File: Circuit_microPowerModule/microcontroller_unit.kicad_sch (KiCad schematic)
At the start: 34 parts, among them J1 USB_C_Receptacle_USB2.0, J5 Debug, SW2 KMR2, SW3 KMR2, U6 RP2040, U9 W25Q128JVS, Y1 12MHz

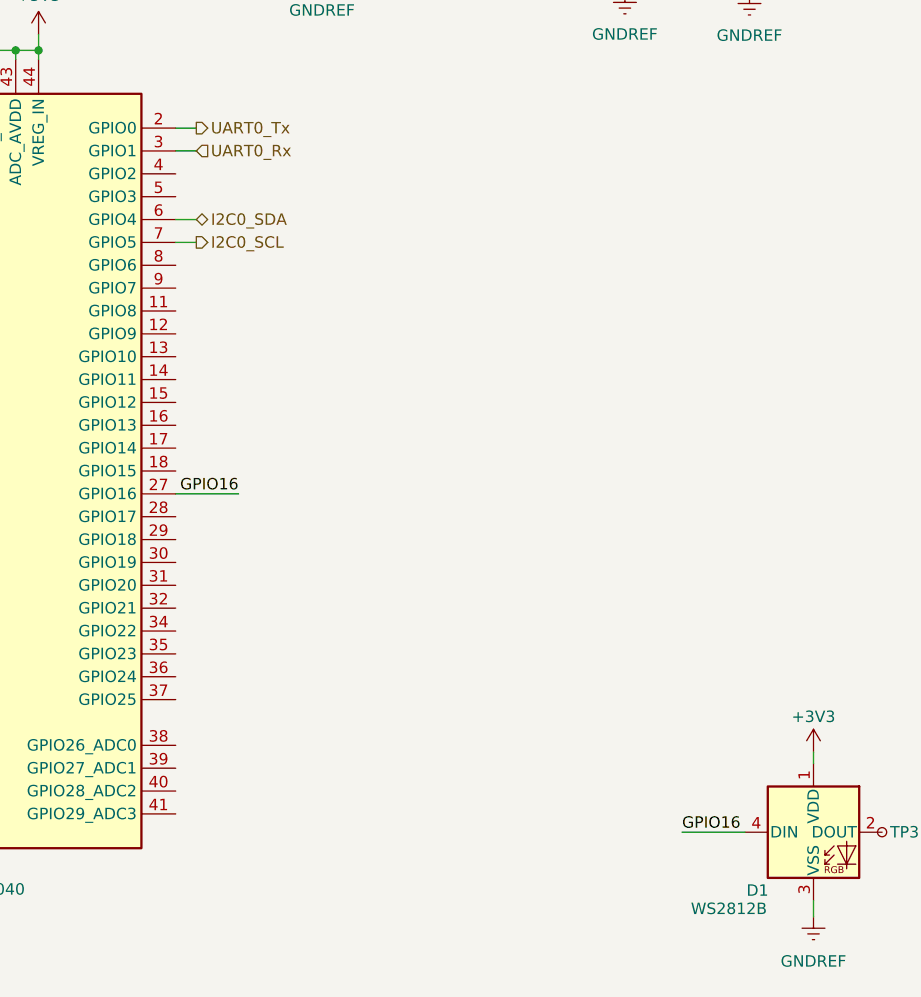
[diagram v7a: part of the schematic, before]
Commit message: define mcu pinout to mikrobus
update hw block diagram file type
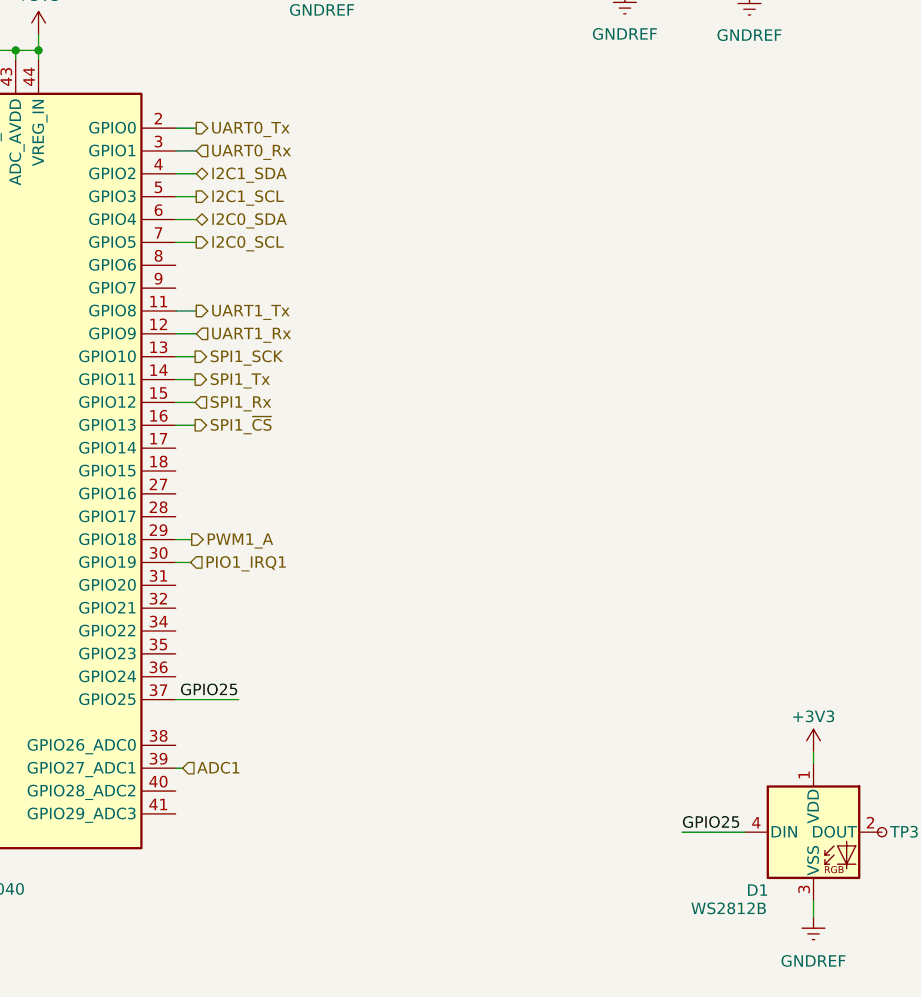
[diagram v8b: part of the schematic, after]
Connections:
- net UART1_Tx: now reaches U6.11 (GPIO8)
- net UART1_Rx: now reaches U6.12 (GPIO9)
- net SPI1_SCK: now reaches U6.13 (GPIO10)
- net SPI1_Tx: now reaches U6.14 (GPIO11)
- net SPI1_Rx: now reaches U6.15 (GPIO12)
- net SPI1_~{CS}: now reaches U6.16 (GPIO13)
- net PWM1_A: now reaches U6.29 (GPIO18)
- net PIO1_IRQ1: now reaches U6.30 (GPIO19)
- net GPIO25: now reaches U6.37 (GPIO25)
- net GPIO25: now also D1.4 (DIN)
- net ADC1: now reaches U6.39 (GPIO27_ADC1)
- net I2C1_SDA: now reaches U6.4 (GPIO2)
- net I2C1_SCL: now reaches U6.5 (GPIO3)
- net GPIO16: no longer names the net of U6.27 (GPIO16)
- net GPIO16: no longer D1.4 (DIN)
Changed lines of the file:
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@@
+    (stroke (width 0) (type default))
+  )
+  (wire (pts (xy 195.834 71.374) (xy 198.12 71.374))
     (stroke (width 0) (type default))
   )
@@
     (stroke (width 0) (type default))
   )
+  (wire (pts (xy 195.834 84.074) (xy 197.993 84.074))
+    (stroke (width 0) (type default))
+  )
   (wire (pts (xy 60.96 119.38) (xy 72.009 119.38))
     (stroke (width 0) (type default))
@@
     (stroke (width 0) (type default))
   )
+  (wire (pts (xy 195.834 96.774) (xy 197.612 96.774))
+    (stroke (width 0) (type default))
+  )
   (wire (pts (xy 161.29 24.13) (xy 165.1 24.13))
     (stroke (width 0) (type default))
@@
     (stroke (width 0) (type default))
   )
+  (wire (pts (xy 195.834 81.534) (xy 197.993 81.534))
+    (stroke (width 0) (type default))
+  )
   (wire (pts (xy 60.96 121.92) (xy 72.009 121.92))
     (stroke (width 0) (type default))
@@
     (stroke (width 0) (type default))
   )
+  (wire (pts (xy 195.834 58.674) (xy 198.12 58.674))
+    (stroke (width 0) (type default))
+  )
   (wire (pts (xy 151.13 24.13) (xy 157.48 24.13))
     (stroke (width 0) (type default))
@@
     (stroke (width 0) (type default))
   )
+  (wire (pts (xy 195.834 73.914) (xy 198.12 73.914))
+    (stroke (width 0) (type default))
+  )
   (wire (pts (xy 48.895 23.368) (xy 48.895 24.765))
     (stroke (width 0) (type default))
@@
     (stroke (width 0) (type default))
   )
+  (wire (pts (xy 195.834 122.174) (xy 196.596 122.174))
+    (stroke (width 0) (type default))
+  )
+  (wire (pts (xy 195.834 56.134) (xy 198.12 56.134))
+    (stroke (width 0) (type default))
+  )
   (wire (pts (xy 151.13 22.86) (xy 151.13 24.13))
     (stroke (width 0) (type default))
@@
     (stroke (width 0) (type default))
   )
+  (wire (pts (xy 195.834 78.994) (xy 197.993 78.994))
+    (stroke (width 0) (type default))
+  )
   (wire (pts (xy 195.834 51.054) (xy 198.12 51.054))
     (stroke (width 0) (type default))
@@
     (stroke (width 0) (type default))
   )
+  (wire (pts (xy 195.834 99.314) (xy 197.485 99.314))
+    (stroke (width 0) (type default))
+  )
   (wire (pts (xy 60.96 109.22) (xy 61.849 109.22))
     (stroke (width 0) (type default))
@@
     (stroke (width 0) (type default))
   )
+  (wire (pts (xy 195.834 76.454) (xy 197.993 76.454))
+    (stroke (width 0) (type default))
+  )
   (wire (pts (xy 151.13 31.75) (xy 157.48 31.75))
     (stroke (width 0) (type default))
@@
     (stroke (width 0) (type default))
   )
+  (wire (pts (xy 195.834 114.554) (xy 202.819 114.554))
+    (stroke (width 0) (type default))
+  )
   (wire (pts (xy 145.034 119.634) (xy 137.16 119.634))
     (stroke (width 0) (type default))
@@
   )
   (wire (pts (xy 157.48 31.75) (xy 161.29 31.75))
-    (stroke (width 0) (type default))
-  )
-  (wire (pts (xy 195.834 91.694) (xy 202.819 91.694))
     (stroke (width 0) (type default))
   )
@@
     (effects (font (size 1.27 1.27)) (justify left bottom))
   )
-  (label "GPIO16" (at 202.819 91.694 180) (fields_autoplaced)
-    (effects (font (size 1.27 1.27)) (justify right bottom))
-  )
   (label "SWDIO" (at 137.16 119.634 0) (fields_autoplaced)
     (effects (font (size 1.27 1.27)) (justify left bottom))
@@
     (effects (font (size 1.27 1.27)) (justify right bottom))
   )
-  (label "GPIO16" (at 252.095 129.286 0) (fields_autoplaced)
+  (label "GPIO25" (at 252.095 129.286 0) (fields_autoplaced)
     (effects (font (size 1.27 1.27)) (justify left bottom))
   )
@@
     (effects (font (size 1.27 1.27)) (justify right bottom))
   )
+  (label "GPIO25" (at 202.819 114.554 180) (fields_autoplaced)
+    (effects (font (size 1.27 1.27)) (justify right bottom))
+  )
   (label "QSPI_NSS" (at 133.985 68.834 0) (fields_autoplaced)
     (effects (font (size 1.27 1.27)) (justify left bottom))
@@
     (effects (font (size 1.27 1.27)) (justify right bottom))
   )
+  (hierarchical_label "UART1_Rx" (shape input) (at 198.12 73.914 0) (fields_autoplaced)
+    (effects (font (size 1.27 1.27)) (justify left))
+  )
+  (hierarchical_label "ADC1" (shape input) (at 196.596 122.174 0) (fields_autoplaced)
+    (effects (font (size 1.27 1.27)) (justify left))
+  )
+  (hierarchical_label "PIO1_IRQ1" (shape input) (at 197.485 99.314 0) (fields_autoplaced)
+    (effects (font (size 1.27 1.27)) (justify left))
+  )
+  (hierarchical_label "SPI1_SCK" (shape output) (at 197.993 76.454 0) (fields_autoplaced)
+    (effects (font (size 1.27 1.27)) (justify left))
+  )
+  (hierarchical_label "SPI1_Rx" (shape input) (at 197.993 81.534 0) (fields_autoplaced)
+    (effects (font (size 1.27 1.27)) (justify left))
+  )
+  (hierarchical_label "UART1_Tx" (shape output) (at 198.12 71.374 0) (fields_autoplaced)
+    (effects (font (size 1.27 1.27)) (justify left))
+  )
+  (hierarchical_label "I2C1_SDA" (shape bidirectional) (at 198.12 56.134 0) (fields_autoplaced)
+    (effects (font (size 1.27 1.27)) (justify left))
+  )
+  (hierarchical_label "SPI1_~{CS}" (shape output) (at 197.993 84.074 0) (fields_autoplaced)
+    (effects (font (size 1.27 1.27)) (justify left))
+  )
+  (hierarchical_label "I2C1_SCL" (shape output) (at 198.12 58.674 0) (fields_autoplaced)
+    (effects (font (size 1.27 1.27)) (justify left))
+  )
+  (hierarchical_label "PWM1_A" (shape output) (at 197.612 96.774 0) (fields_autoplaced)
+    (effects (font (size 1.27 1.27)) (justify left))
+  )
   (hierarchical_label "I2C0_SDA" (shape bidirectional) (at 198.12 61.214 0) (fields_autoplaced)
     (effects (font (size 1.27 1.27)) (justify left))
@@
     (effects (font (size 1.27 1.27)) (justify left))
   )
+  (hierarchical_label "SPI1_Tx" (shape output) (at 197.993 78.994 0) (fields_autoplaced)
+    (effects (font (size 1.27 1.27)) (justify left))
+  )
